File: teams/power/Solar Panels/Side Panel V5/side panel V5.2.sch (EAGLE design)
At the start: 14 parts

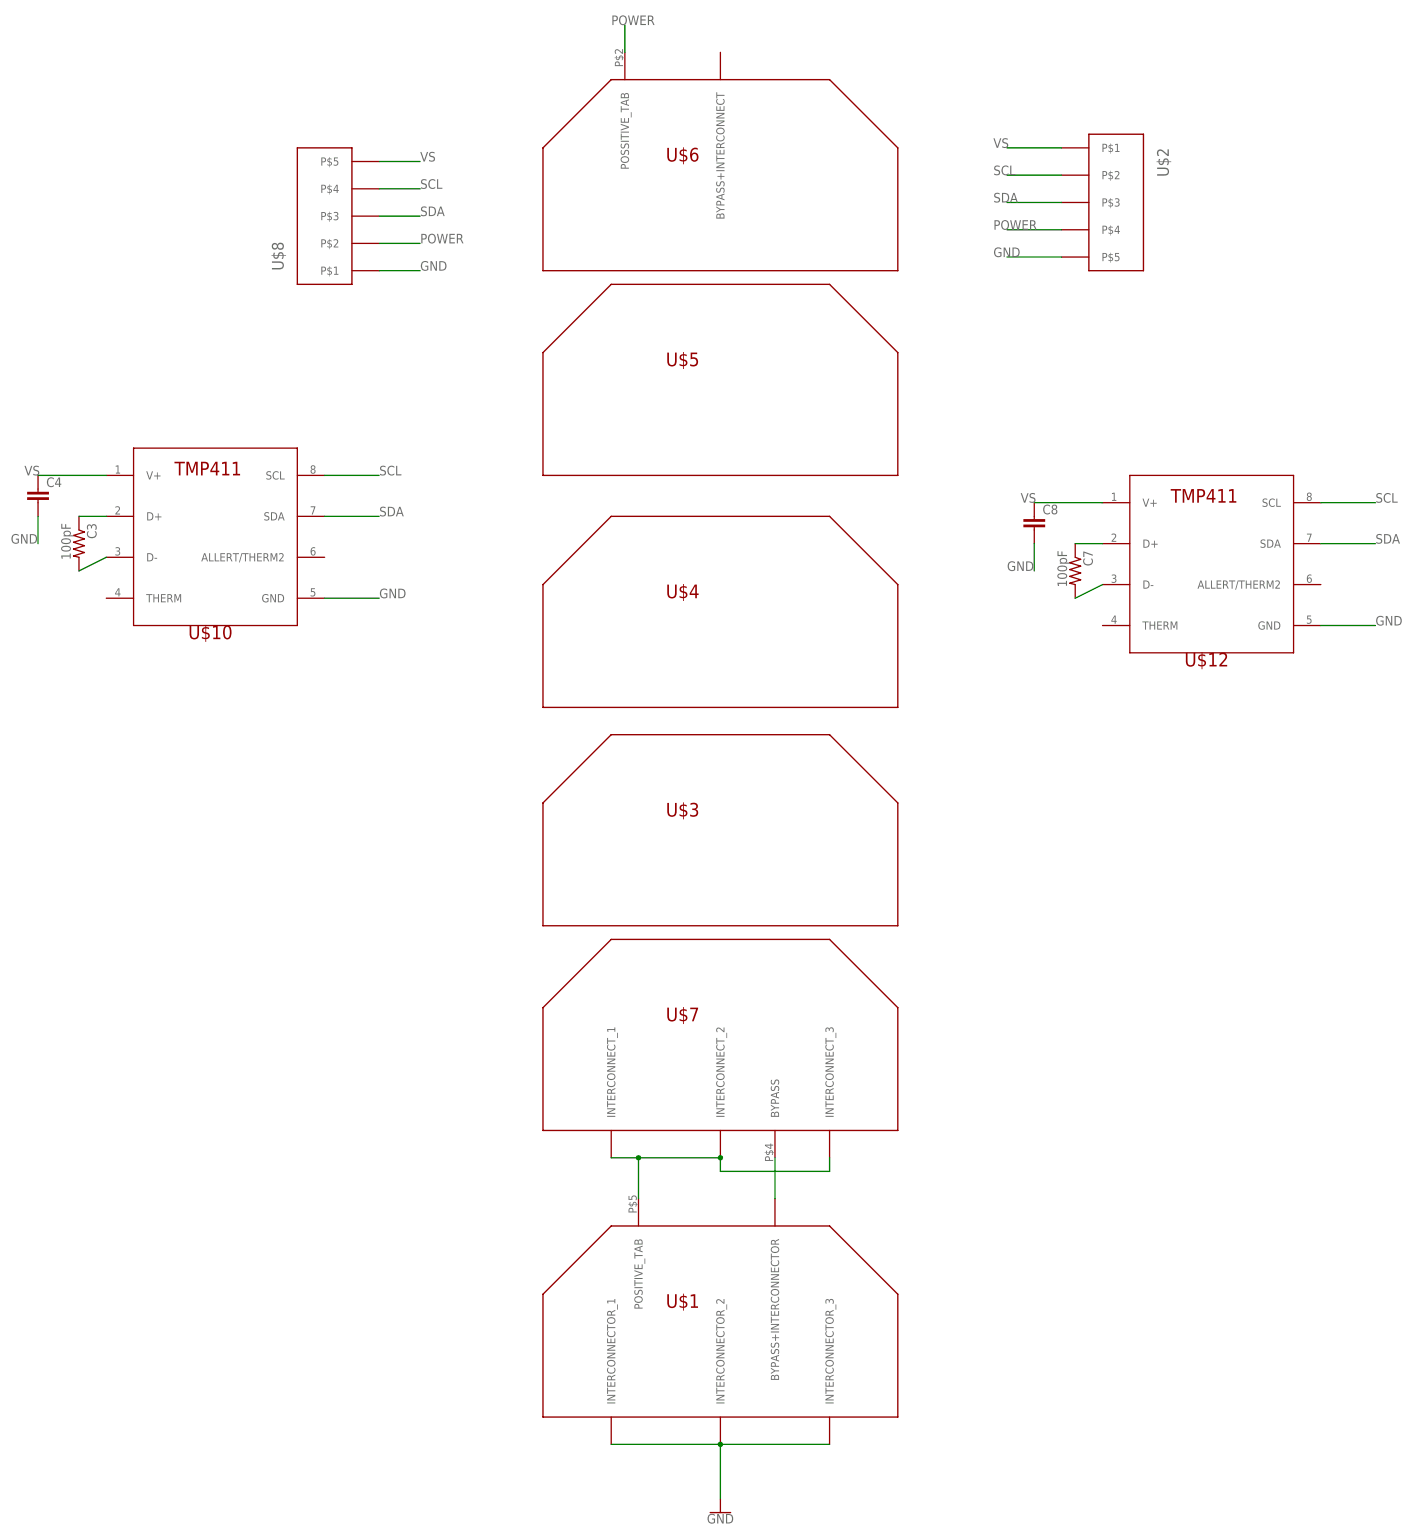
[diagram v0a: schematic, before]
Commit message: EPS/ old panels: Remove ground plane and changed temp sensor to TMP36
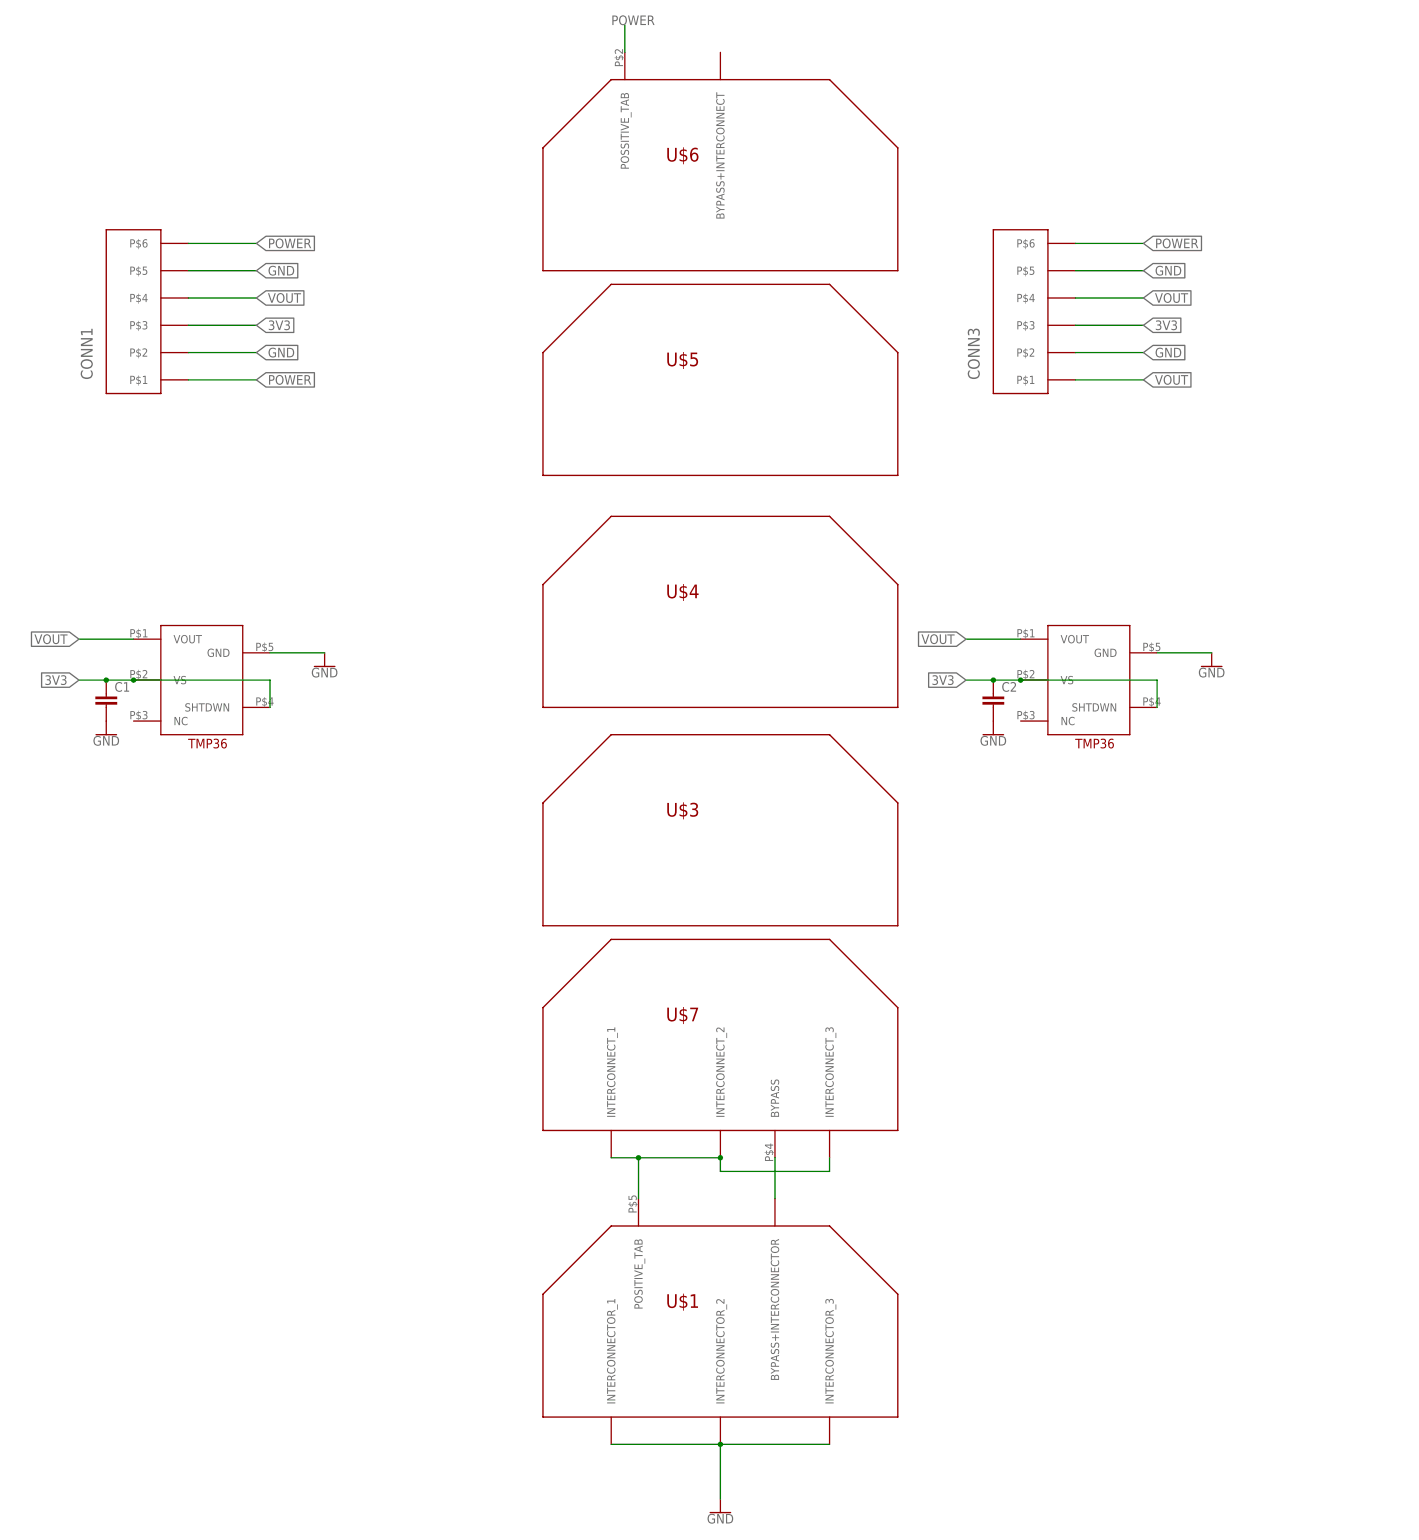
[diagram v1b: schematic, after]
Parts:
- removed C3, C7: 100pF, Battery board V4.1 - simple signals:R-US_R0805
- removed C4, C8: (no value), Battery board V4.1 - simple signals:C
- removed U$10, U$12: TMP411, DubSat1 Components:TMP411
- added C1, C2: (no value), DubSat1 Components:CAPACITOR0805
- added CONN1, CONN3: PICOLOCK_6, DubSat1 Components:PICOLOCK_6
- U$2, U$8: value PICOLOCK_5 -> TMP36; device DubSat1 Components:PICOLOCK_5 -> DubSat1 Components:TMP36
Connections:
- removed net N$13: C3.1, U$10.D+
- removed net N$14: C3.2, U$10.D-
- removed net N$17: C7.1, U$12.D+
- removed net N$18: C7.2, U$12.D-
- removed net SCL: U$10.SCL, U$12.SCL, U$2.P$2, U$8.P$4
- removed net SDA: U$10.SDA, U$12.SDA, U$2.P$3, U$8.P$3
- removed net VS: C4.1, C8.1, U$10.V+, U$12.V+, U$2.P$1, U$8.P$5
- new net 3V3: C1.1, C2.1, CONN1.P$3, CONN3.P$3, U$2.SHTDWN, U$2.VS, U$8.SHTDWN, U$8.VS
- new net VOUT: CONN1.P$4, CONN3.P$1, CONN3.P$4, U$2.VOUT, U$8.VOUT
- net GND: now also C1.2, C2.2, CONN1.P$2, CONN1.P$5, CONN3.P$2, CONN3.P$5, U$2.GND, U$8.GND; no longer C4.2, C8.2, U$10.GND, U$12.GND, U$2.P$5, U$8.P$1
- net POWER: now also CONN1.P$1, CONN1.P$6, CONN3.P$6; no longer U$2.P$4, U$8.P$2
